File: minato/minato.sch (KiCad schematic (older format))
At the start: 212 parts, among them J1 Conn_ARM_JTAG_SWD_10, U2 STM32F103C8Tx

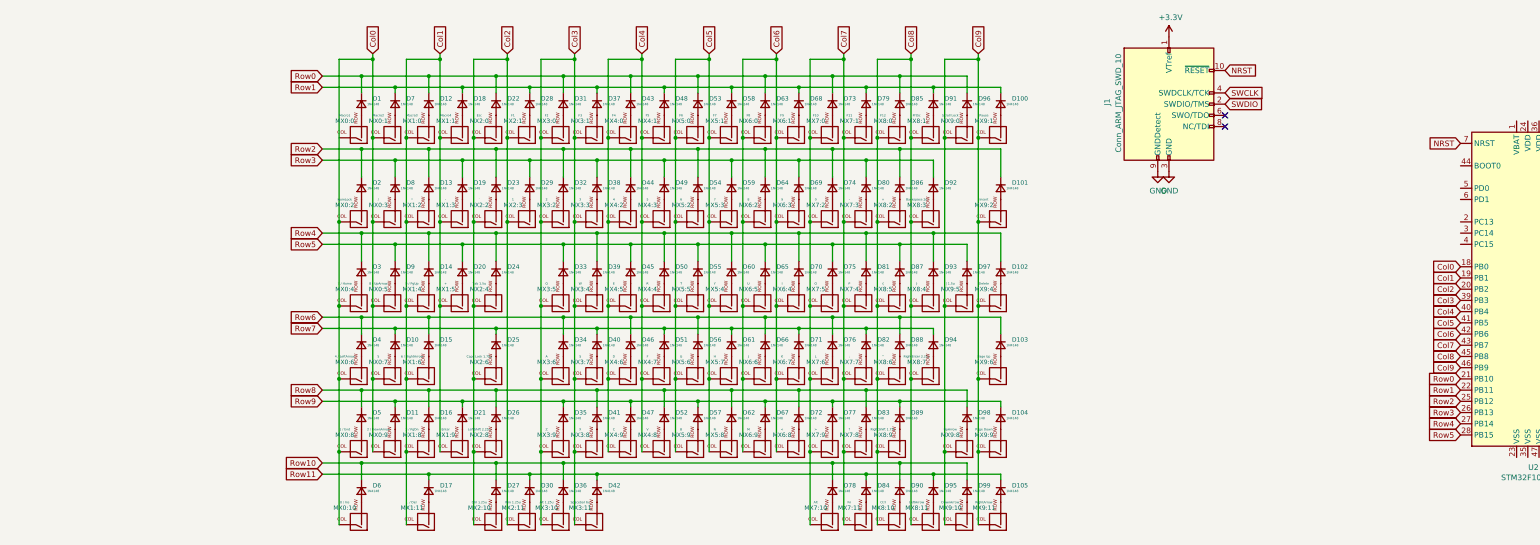
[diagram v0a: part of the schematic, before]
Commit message: :sparkles: Add crystal + HW reset
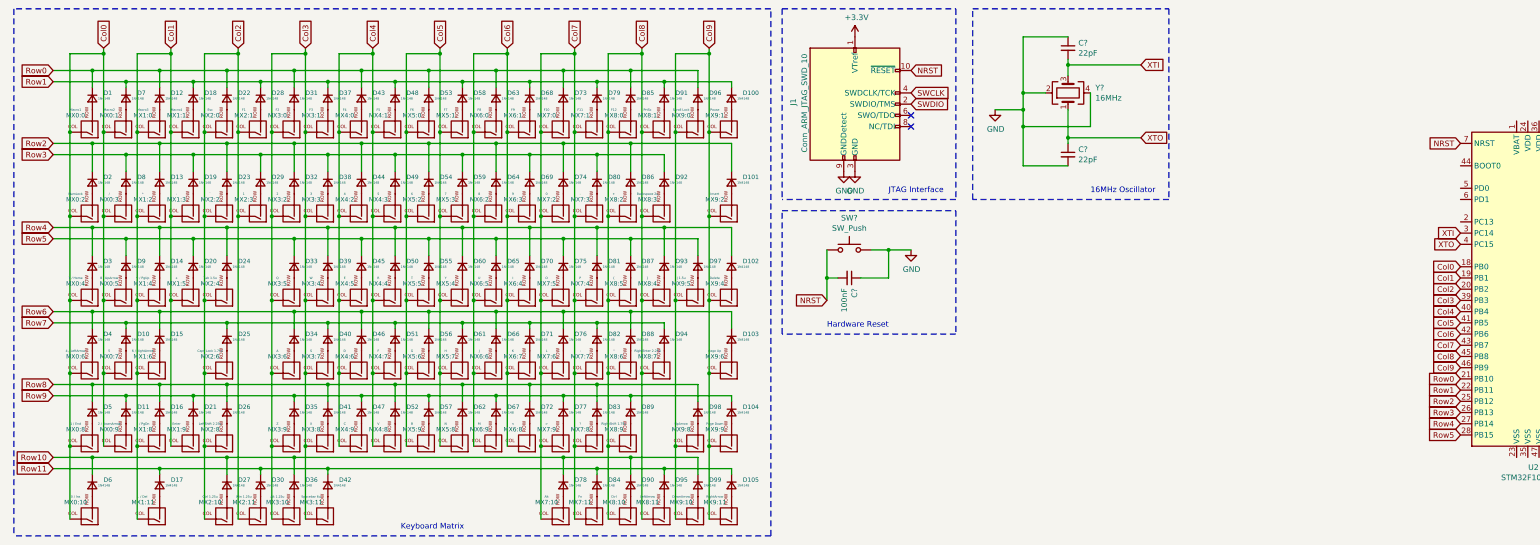
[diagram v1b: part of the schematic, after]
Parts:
- added C? (x2): 22pF, symbol Device:C_Small
- added C?: 100nF, symbol Device:C_Small
- added SW?: SW_Push, symbol Switch:SW_Push
- added Y?: 16MHz, symbol Device:Crystal_GND24
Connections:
- net Col0: now also MX0:0.1 (COL)
- net GND: now also C?.1, C?.1, C?.2, SW?.2, Y?.2, Y?.4
- net NRST: now also C?.2, SW?.1
- net XTI: now reaches U2.3 (PC14)
- net XTI: now also C?.2, Y?.3
- net XTO: now reaches U2.4 (PC15)
- net XTO: now also C?.1, Y?.1
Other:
- note added: "16MHz Oscillator"
- note added: "Hardware Reset"
- note added: "JTAG Interface"
- note added: "Keyboard Matrix"
- moved on the sheet: D1, D10, D100, D101, D102, D103, D104, D105, D11, D12, D13, D14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

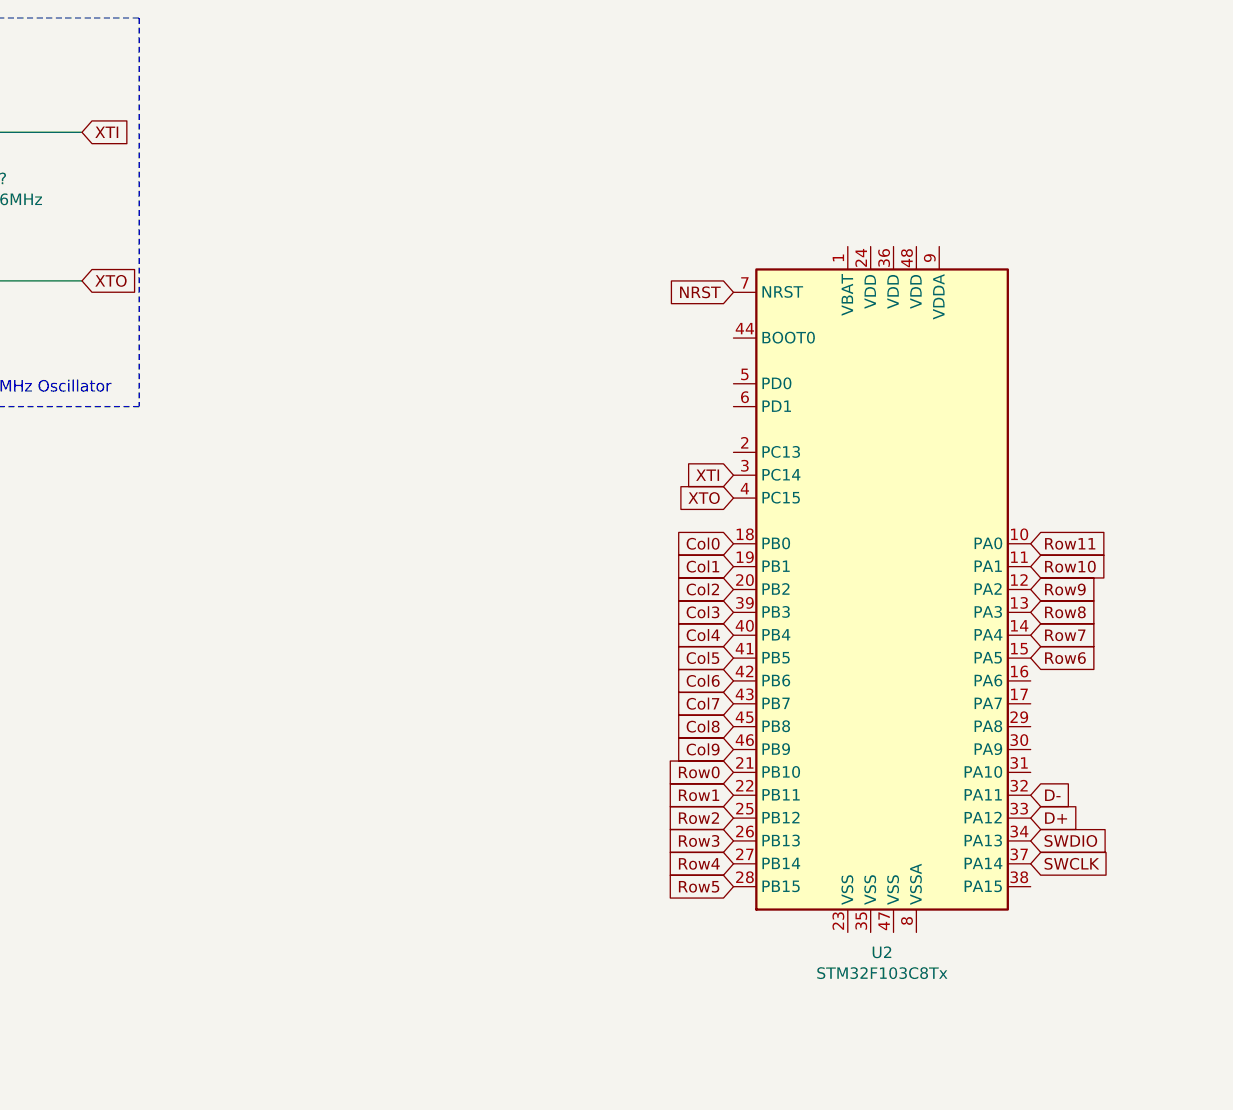
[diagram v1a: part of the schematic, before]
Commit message: :sparkles: Add decoupler
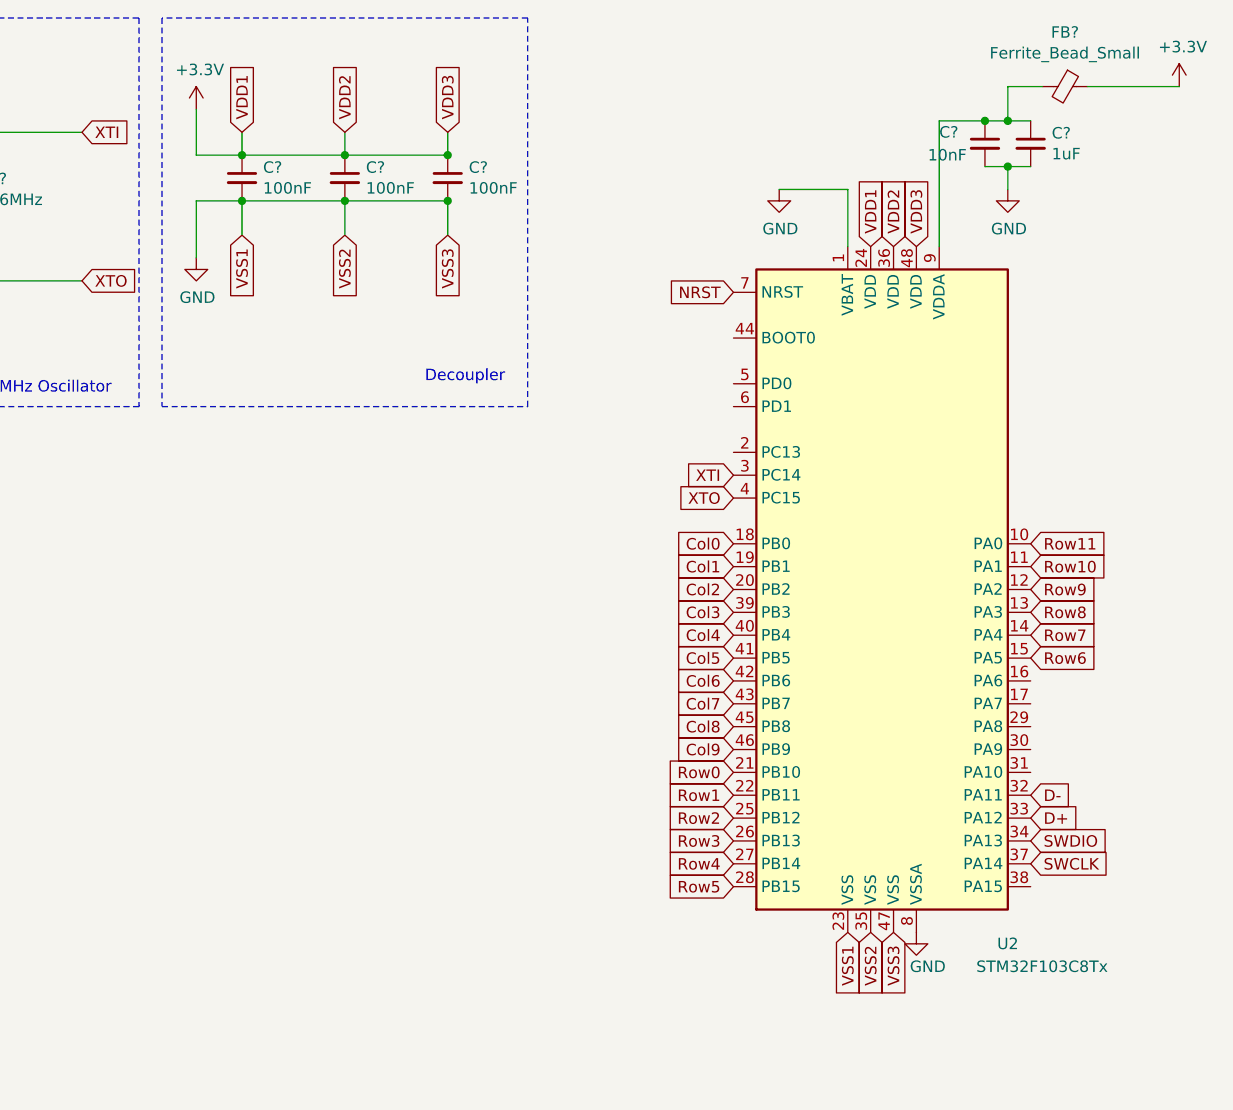
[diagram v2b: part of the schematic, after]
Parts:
- added C?: 10nF, symbol Device:C_Small
- added C?: 1uF, symbol Device:C_Small
- added C? (x3): 100nF, symbol Device:C_Small
- added FB?: Ferrite_Bead_Small, symbol Device:Ferrite_Bead_Small
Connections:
- net +3V3: now also U2.24 (VDD), U2.36 (VDD), U2.48 (VDD), C?.1, C?.1, C?.1, FB?.1
- net GND: now also U2.1 (VBAT), U2.23 (VSS), U2.35 (VSS), U2.47 (VSS), U2.8 (VSSA), C?.2, C?.2, C?.2, C?.2, C?.2
- net at U2.9 (VDDA): now also C?.1, C?.1, FB?.2
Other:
- note added: "Decoupler"
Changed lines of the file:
@@
 U 1 1 5E445AE3
 P 14150 3050
-F 0 "U2" H 14100 1461 50  0000 C CNN
-F 1 "STM32F103C8Tx" H 14100 1370 50  0000 C CNN
+F 0 "U2" H 14650 1500 50  0000 C CNN
+F 1 "STM32F103C8Tx" H 14800 1400 50  0000 C CNN
 F 2 "Package_QFP:LQFP-48_7x7mm_P0.5mm" H 13550 1650 50  0001 R CNN
 F 3 "http://www.st.com/st-web-ui/static/active/en/resource/technical/document/datasheet/CD00161566.pdf" H 14150 3050 50  0001 C CNN
@@
 Wire Notes Line
 	7400 3450 7400 2350
+$Comp
+L power:GND #PWR?
+U 1 1 5EB54336
+P 13650 1300
+F 0 "#PWR?" H 13650 1050 50  0001 C CNN
+F 1 "GND" H 13655 1127 50  0000 C CNN
+F 2 "" H 13650 1300 50  0001 C CNN
+F 3 "" H 13650 1300 50  0001 C CNN
+	1    13650 1300
+	1    0    0    -1
+$EndComp
+Wire Wire Line
+	13950 1550 13950 1300
+Wire Wire Line
+	13950 1300 13650 1300
+$Comp
+L Device:C_Small C?
+U 1 1 5EB7A453
+P 14550 1100
+F 0 "C?" H 14350 1150 50  0000 L CNN
+F 1 "10nF" H 14300 1050 50  0000 L CNN
+F 2 "" H 14550 1100 50  0001 C CNN
+F 3 "~" H 14550 1100 50  0001 C CNN
+	1    14550 1100
+	1    0    0    -1
+$EndComp
+$Comp
+L Device:C_Small C?
+U 1 1 5EB7A7E6
+P 14750 1100
+F 0 "C?" H 14842 1146 50  0000 L CNN
+F 1 "1uF" H 14842 1055 50  0000 L CNN
+F 2 "" H 14750 1100 50  0001 C CNN
+F 3 "~" H 14750 1100 50  0001 C CNN
+	1    14750 1100
+	1    0    0    -1
+$EndComp
+$Comp
+L Device:Ferrite_Bead_Small FB?
+U 1 1 5EB7C88F
+P 14900 850
+F 0 "FB?" V 14663 850 50  0000 C CNN
+F 1 "Ferrite_Bead_Small" V 14754 850 50  0000 C CNN
+F 2 "" V 14830 850 50  0001 C CNN
+F 3 "~" H 14900 850 50  0001 C CNN
+	1    14900 850
+	0    1    1    0
+$EndComp
+$Comp
+L power:+3.3V #PWR?
+U 1 1 5EB810BA
+P 15400 850
+F 0 "#PWR?" H 15400 700 50  0001 C CNN
+F 1 "+3.3V" H 15415 1023 50  0000 C CNN
+F 2 "" H 15400 850 50  0001 C CNN
+F 3 "" H 15400 850 50  0001 C CNN
+	1    15400 850
+	1    0    0    -1
+$EndComp
+Wire Wire Line
+	14550 1000 14650 1000
+$Comp
+L power:GND #PWR?
+U 1 1 5EBEEF68
+P 14650 1300
+F 0 "#PWR?" H 14650 1050 50  0001 C CNN
+F 1 "GND" H 14655 1127 50  0000 C CNN
+F 2 "" H 14650 1300 50  0001 C CNN
+F 3 "" H 14650 1300 50  0001 C CNN
+	1    14650 1300
+	1    0    0    -1
+$EndComp
+Wire Wire Line
+	14550 1200 14650 1200
+Wire Wire Line
+	14650 1200 14650 1300
+Connection ~ 14650 1200
+Wire Wire Line
+	14650 1200 14750 1200
+Wire Wire Line
+	14650 1000 14650 850
+Wire Wire Line
+	14650 850  14800 850
+Connection ~ 14650 1000
+Wire Wire Line
+	14650 1000 14750 1000
+Wire Wire Line
+	15000 850  15400 850
+Wire Wire Line
+	14350 1550 14350 1000
+Wire Wire Line
+	14350 1000 14550 1000
+Connection ~ 14550 1000
+Text GLabel 14050 1550 1    50   Input ~ 0
+VDD1
+Text GLabel 14150 1550 1    50   Input ~ 0
+VDD2
+Text GLabel 14250 1550 1    50   Input ~ 0
+VDD3
+Text GLabel 13950 4550 3    50   Input ~ 0
+VSS1
+Text GLabel 14050 4550 3    50   Input ~ 0
+VSS2
+Text GLabel 14150 4550 3    50   Input ~ 0
+VSS3
+$Comp
+L power:GND #PWR?
+U 1 1 5ECB4161
+P 14250 4550
+F 0 "#PWR?" H 14250 4300 50  0001 C CNN
+F 1 "GND" H 14300 4400 50  0000 C CNN
+F 2 "" H 14250 4550 50  0001 C CNN
+F 3 "" H 14250 4550 50  0001 C CNN
+	1    14250 4550
+	1    0    0    -1
+$EndComp
+$Comp
+L Device:C_Small C?
+U 1 1 5ECB8B35
+P 11300 1250
+F 0 "C?" H 11392 1296 50  0000 L CNN
+F 1 "100nF" H 11392 1205 50  0000 L CNN
+F 2 "" H 11300 1250 50  0001 C CNN
+F 3 "~" H 11300 1250 50  0001 C CNN
+	1    11300 1250
+	1    0    0    -1
+$EndComp
+$Comp
+L Device:C_Small C?
+U 1 1 5ECB9189
+P 11750 1250
+F 0 "C?" H 11842 1296 50  0000 L CNN
+F 1 "100nF" H 11842 1205 50  0000 L CNN
+F 2 "" H 11750 1250 50  0001 C CNN
+F 3 "~" H 11750 1250 50  0001 C CNN
+	1    11750 1250
+	1    0    0    -1
+$EndComp
+$Comp
+L Device:C_Small C?
+U 1 1 5ECB9680
+P 12200 1250
+F 0 "C?" H 12292 1296 50  0000 L CNN
+F 1 "100nF" H 12292 1205 50  0000 L CNN
+F 2 "" H 12200 1250 50  0001 C CNN
+F 3 "~" H 12200 1250 50  0001 C CNN
+	1    12200 1250
+	1    0    0    -1
+$EndComp
+$Comp
+L power:+3.3V #PWR?
+U 1 1 5ECBBF30
+P 11100 950
+F 0 "#PWR?" H 11100 800 50  0001 C CNN
+F 1 "+3.3V" H 11115 1123 50  0000 C CNN
+F 2 "" H 11100 950 50  0001 C CNN
+F 3 "" H 11100 950 50  0001 C CNN
+	1    11100 950
+	1    0    0    -1
+$EndComp
+Wire Wire Line
+	11100 950  11100 1150
+Wire Wire Line
+	11100 1150 11300 1150
+Connection ~ 11300 1150
+Wire Wire Line
+	11300 1150 11750 1150
+Connection ~ 11750 1150
+Wire Wire Line
+	11750 1150 12200 1150
+Text GLabel 11300 1050 1    50   Input ~ 0
+VDD1
+Text GLabel 11750 1050 1    50   Input ~ 0
+VDD2
+Text GLabel 12200 1050 1    50   Input ~ 0
+VDD3
+$Comp
+L power:GND #PWR?
+U 1 1 5ECECA6D
+P 11100 1600
+F 0 "#PWR?" H 11100 1350 50  0001 C CNN
+F 1 "GND" H 11105 1427 50  0000 C CNN
+F 2 "" H 11100 1600 50  0001 C CNN
+F 3 "" H 11100 1600 50  0001 C CNN
+	1    11100 1600
+	1    0    0    -1
+$EndComp
+Wire Wire Line
+	12200 1350 11750 1350
+Wire Wire Line
+	11100 1350 11100 1600
+Connection ~ 11300 1350
+Wire Wire Line
+	11300 1350 11100 1350
+Connection ~ 11750 1350
+Wire Wire Line
+	11750 1350 11300 1350
+Wire Wire Line
+	11300 1050 11300 1150
+Wire Wire Line
+	11750 1050 11750 1150
+Wire Wire Line
+	12200 1050 12200 1150
+Connection ~ 12200 1150
+Text GLabel 11300 1500 3    50   Input ~ 0
+VSS1
+Text GLabel 11750 1500 3    50   Input ~ 0
+VSS2
+Text GLabel 12200 1500 3    50   Input ~ 0
+VSS3
+Wire Wire Line
+	11300 1500 11300 1350
+Wire Wire Line
+	11750 1500 11750 1350
+Wire Wire Line
+	12200 1500 12200 1350
+Connection ~ 12200 1350
+Text Notes 12100 2150 0    50   ~ 0
+Decoupler
+Wire Notes Line
+	10950 550  10950 2250
+Wire Notes Line
+	10950 2250 12550 2250
+Wire Notes Line
+	12550 2250 12550 550
+Wire Notes Line
+	12550 550  10950 550
 $EndSCHEMATC

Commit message: :sparkles: Add USB-C receptacle
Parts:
- removed C?: 100nF, symbol Device:C_Small
- removed SW?: SW_Push, symbol Switch:SW_Push
- added C?: 10uF, symbol Device:C_Small
- added C? (x2): 4.7nF, symbol Device:C_Small
- added D?: 1N4148, Diode_THT:D_DO-35_SOD27_P7.62mm_Horizontal, symbol Diode:1N4148
- added J?: USB_C_Receptacle_USB2.0, symbol Connector:USB_C_Receptacle_USB2.0
- added Q?: DTC123J, symbol Transistor_BJT:DTC123J
- added R?: 10k, symbol Device:R_Small
- added R?: 1M, symbol Device:R_Small
- added R? (x2): 5.1k, symbol Device:R_Small
- added SW?: SW_Push, symbol Switch:SW_Push
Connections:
- net +3V3: no longer C?.1, C?.1, C?.1, FB?.1, U2.24 (VDD), U2.36 (VDD), U2.48 (VDD)
- net GND: now also C?.1, C?.2, C?.2, J?.A1 (GND), J?.A12 (GND), J?.B1 (GND), J?.B12 (GND), Q?.3 (C), R?.1, R?.1, R?.2, R?.2
- net NRST: now also C?.1, Q?.2 (E)
- net BOOT0: now reaches U2.44 (BOOT0)
- net BOOT0: now also C?.2, D?.1 (K), R?.1
- new net: D?.2 (A), Q?.1 (B), SW?.2
- new net: C?.1, J?.S1 (SHIELD), R?.1
- new net: J?.A5 (CC1), R?.2
- new net: J?.B5 (CC2), R?.2
- new net 3.3V: C?.1, C?.1, C?.1, FB?.1, SW?.1, U2.24 (VDD), U2.36 (VDD), U2.48 (VDD)
- new net DBUS+: J?.A6 (D+), J?.B6 (D+)
- new net DBUS-: J?.A7 (D-), J?.B7 (D-)
- new net VBUS: J?.A4 (VBUS), J?.A9 (VBUS), J?.B4 (VBUS), J?.B9 (VBUS)
- no-connect marks 2 -> 4
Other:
- note added: "Decoupling capacitors"
- note added: "USB C Receptacle"
- note removed: "Decoupler"

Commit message: :sparkles: Assign footprints
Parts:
- removed C? (x2): 22pF, symbol Device:C_Small
- removed FB?: Ferrite_Bead_Small, symbol Device:Ferrite_Bead_Small
- removed Y?: 16MHz, symbol Device:Crystal_GND24
- added C6, C8: 100nF, keyboard_parts.pretty:C_3225, symbol Device:C_Small
- added D108: 1N4148, keyboard_parts.pretty:D_SOD123W_hand, symbol Diode:1N4148
- added F1: Polyfuse_Small, Fuse:Fuse_1812_4532Metric, symbol Device:Polyfuse_Small
- added U1: MCP1700-3302E_SOT23, Package_TO_SOT_SMD:SOT-23, symbol Regulator_Linear:MCP1700-3302E_SOT23
- added Y1: 16MHz, local.pretty:OSC_CSTCE16M0V53-R0, symbol CSTCE16M0V53-R0:CSTCE16M0V53-R0
- C1, C10, C11, C12, C2, C3, C7, C9: renamed from C?; footprint (none) -> keyboard_parts.pretty:C_3225
- D1, D10, D100, D101, D102, D103, D104, D105, D11, D12, D13, D14, D15, D16, D17, D18, D19, D2, D20, D21, D22, D23, D24, D25, D26, D27, D28, D29, D3, D30, D31, D32, D33, D34, D35, D36, D37, D38, D39, D4, D40, D41, D42, D43, D44, D45, D46, D47, D48, D49, D5, D50, D51, D52, D53, D54, D55, D56, D57, D58, D59, D6, D60, D61, D62, D63, D64, D65, D66, D67, D68, D69, D7, D70, D71, D72, D73, D74, D75, D76, D77, D78, D79, D8, D80, D81, D82, D83, D84, D85, D86, D87, D88, D89, D9, D90, D91, D92, D93, D94, D95, D96, D97, D98, D99: footprint Diode_SMD:D_SOD-123 -> keyboard_parts.pretty:D_SOD123W_hand
- D106: renamed from D?; footprint Diode_THT:D_DO-35_SOD27_P7.62mm_Horizontal -> keyboard_parts.pretty:D_SOD123W_hand
- J1: footprint (none) -> Connector_IDC:IDC-Header_2x05_P2.54mm_Vertical
- J2: renamed from J?; footprint (none) -> Connector_USB:USB_C_Receptacle_GCT_USB4085
- Q1: renamed from Q?; footprint (none) -> Package_TO_SOT_SMD:SOT-23
- R1, R2, R3, R4: renamed from R?; footprint (none) -> keyboard_parts.pretty:R_2012
- SW1: renamed from SW?; footprint (none) -> keyboard_parts.pretty:SW_TACT_TH_HORIZ
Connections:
- net 3.3V: now also C11.1, C12.1, U2.9 (VDDA), C8.1, D108.2 (A), U1.2 (VO)
- net GND: now also C6.2, C8.2, U1.1 (GND), Y1.2 (GND)
- net VBUS: now also F1.2
- net XTI: now also Y1.1 (IN)
- net XTO: now also Y1.3 (OUT)
- new net 5V: C6.1, D108.1 (K), F1.1, U1.3 (VI)
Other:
- note added: "Power Supply"

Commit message: :construction: WIP
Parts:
- C1, C10, C11, C12, C2, C3, C6, C7, C8, C9: footprint keyboard_parts.pretty:C_3225 -> Capacitor_SMD:C_0805_2012Metric
- SW1: footprint keyboard_parts.pretty:SW_TACT_TH_HORIZ -> keyboard_parts.pretty:SW_ALPS_SKRP
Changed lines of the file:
@@
 F 0 "C7" H 11392 1296 50  0000 L CNN
 F 1 "100nF" H 11392 1205 50  0000 L CNN
-F 2 "keyboard_parts.pretty:C_3225" H 11300 1250 50  0001 C CNN
+F 2 "Capacitor_SMD:C_0805_2012Metric" H 11300 1250 50  0001 C CNN
 F 3 "~" H 11300 1250 50  0001 C CNN
 	1    11300 1250
@@
 F 0 "C9" H 11842 1296 50  0000 L CNN
 F 1 "100nF" H 11842 1205 50  0000 L CNN
-F 2 "keyboard_parts.pretty:C_3225" H 11750 1250 50  0001 C CNN
+F 2 "Capacitor_SMD:C_0805_2012Metric" H 11750 1250 50  0001 C CNN
 F 3 "~" H 11750 1250 50  0001 C CNN
 	1    11750 1250
@@
 F 0 "C10" H 12292 1296 50  0000 L CNN
 F 1 "100nF" H 12292 1205 50  0000 L CNN
-F 2 "keyboard_parts.pretty:C_3225" H 12200 1250 50  0001 C CNN
+F 2 "Capacitor_SMD:C_0805_2012Metric" H 12200 1250 50  0001 C CNN
 F 3 "~" H 12200 1250 50  0001 C CNN
 	1    12200 1250
@@
 F 0 "SW1" H 7850 3535 50  0000 C CNN
 F 1 "SW_Push" H 7850 3444 50  0000 C CNN
-F 2 "keyboard_parts.pretty:SW_TACT_TH_HORIZ" H 7850 3450 50  0001 C CNN
+F 2 "keyboard_parts.pretty:SW_ALPS_SKRP" H 7850 3450 50  0001 C CNN
 F 3 "~" H 7850 3450 50  0001 C CNN
 	1    7850 3250
@@
 F 0 "C2" H 8608 3404 50  0000 R CNN
 F 1 "10uF" H 8608 3495 50  0000 R CNN
-F 2 "keyboard_parts.pretty:C_3225" H 8700 3450 50  0001 C CNN
+F 2 "Capacitor_SMD:C_0805_2012Metric" H 8700 3450 50  0001 C CNN
 F 3 "~" H 8700 3450 50  0001 C CNN
 	1    8700 3450
@@
 F 0 "C1" H 8542 2796 50  0000 L CNN
 F 1 "4.7nF" H 8542 2705 50  0000 L CNN
-F 2 "keyboard_parts.pretty:C_3225" H 8450 2750 50  0001 C CNN
+F 2 "Capacitor_SMD:C_0805_2012Metric" H 8450 2750 50  0001 C CNN
 F 3 "~" H 8450 2750 50  0001 C CNN
 	1    8450 2750
@@
 F 0 "C3" H 9992 4446 50  0000 L CNN
 F 1 "4.7nF" H 9992 4355 50  0000 L CNN
-F 2 "keyboard_parts.pretty:C_3225" H 9900 4400 50  0001 C CNN
+F 2 "Capacitor_SMD:C_0805_2012Metric" H 9900 4400 50  0001 C CNN
 F 3 "~" H 9900 4400 50  0001 C CNN
 	1    9900 4400
@@
 F 0 "C6" H 11142 6196 50  0000 L CNN
 F 1 "100nF" H 11142 6105 50  0000 L CNN
-F 2 "keyboard_parts.pretty:C_3225" H 11050 6150 50  0001 C CNN
+F 2 "Capacitor_SMD:C_0805_2012Metric" H 11050 6150 50  0001 C CNN
 F 3 "~" H 11050 6150 50  0001 C CNN
 	1    11050 6150
@@
 F 0 "C8" H 11742 6196 50  0000 L CNN
 F 1 "100nF" H 11742 6105 50  0000 L CNN
-F 2 "keyboard_parts.pretty:C_3225" H 11650 6150 50  0001 C CNN
+F 2 "Capacitor_SMD:C_0805_2012Metric" H 11650 6150 50  0001 C CNN
 F 3 "~" H 11650 6150 50  0001 C CNN
 	1    11650 6150
@@
 F 0 "C12" H 14842 1146 50  0000 L CNN
 F 1 "1uF" H 14842 1055 50  0000 L CNN
-F 2 "keyboard_parts.pretty:C_3225" H 14750 1100 50  0001 C CNN
+F 2 "Capacitor_SMD:C_0805_2012Metric" H 14750 1100 50  0001 C CNN
 F 3 "~" H 14750 1100 50  0001 C CNN
 	1    14750 1100
@@
 F 0 "C11" H 14350 1150 50  0000 L CNN
 F 1 "10nF" H 14300 1050 50  0000 L CNN
-F 2 "keyboard_parts.pretty:C_3225" H 14550 1100 50  0001 C CNN
+F 2 "Capacitor_SMD:C_0805_2012Metric" H 14550 1100 50  0001 C CNN
 F 3 "~" H 14550 1100 50  0001 C CNN
 	1    14550 1100
